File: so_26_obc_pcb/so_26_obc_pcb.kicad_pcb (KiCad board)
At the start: 4 copper layers, 90.2 x 95.9 mm, 62 parts, among them J1 Conn_02x12_Odd_Even, J2 Conn_02x06_Odd_Even, J3 Conn_01x04, J4 Conn_01x03, J5 Conn_01x03, J6 Conn_01x02, SW1 SW_Push, U1 STM32G431RBTx, U2 MPRLS0025, U3 PCT2075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

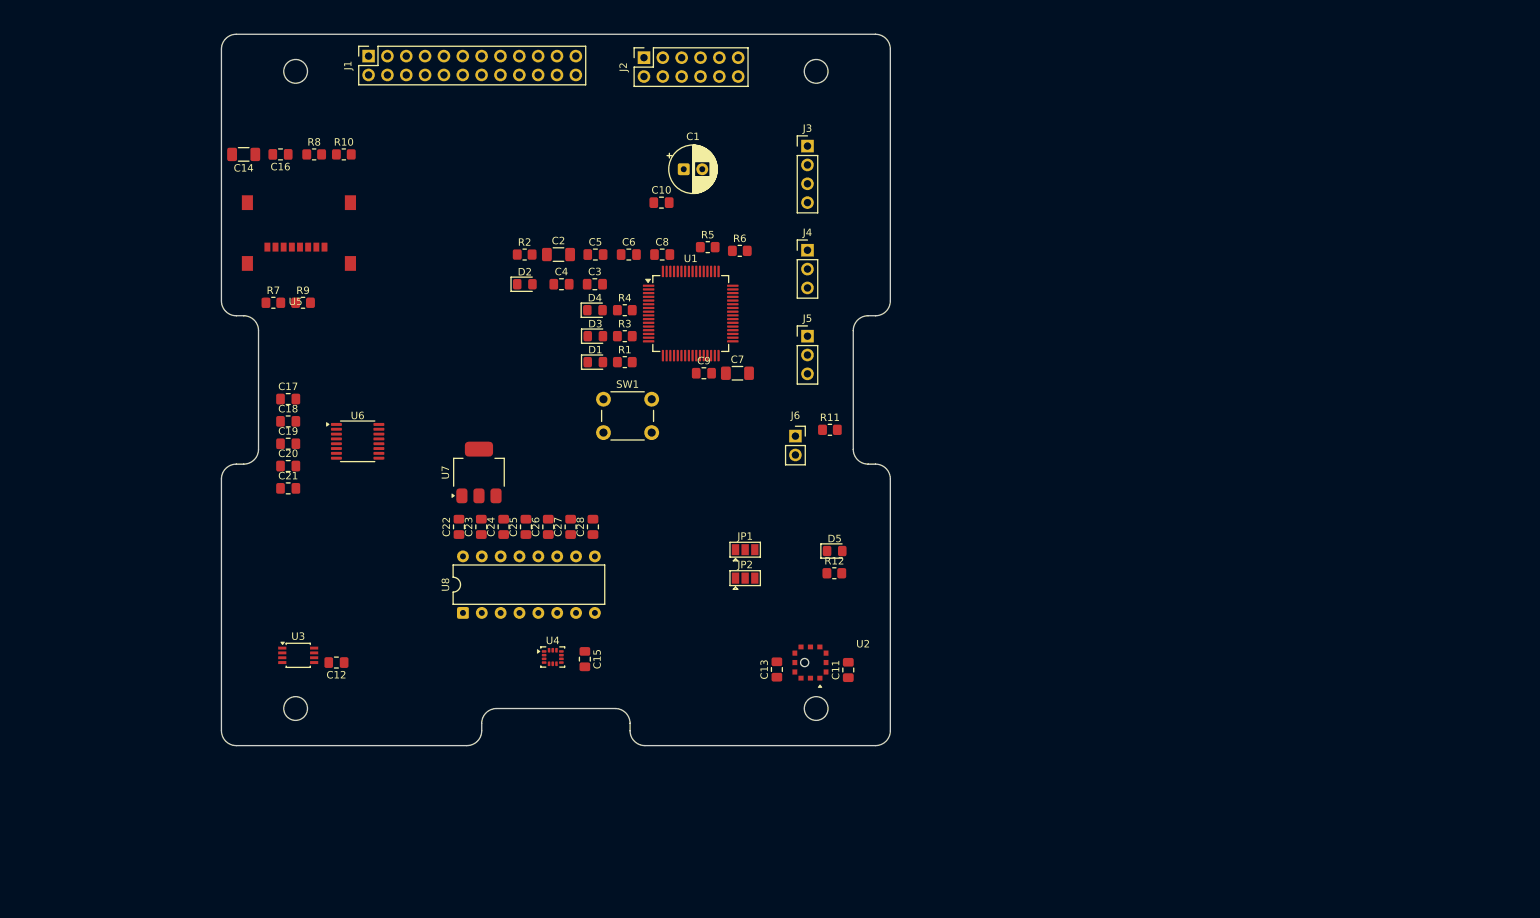
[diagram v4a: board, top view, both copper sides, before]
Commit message: changed back to old rs232 tranceiver
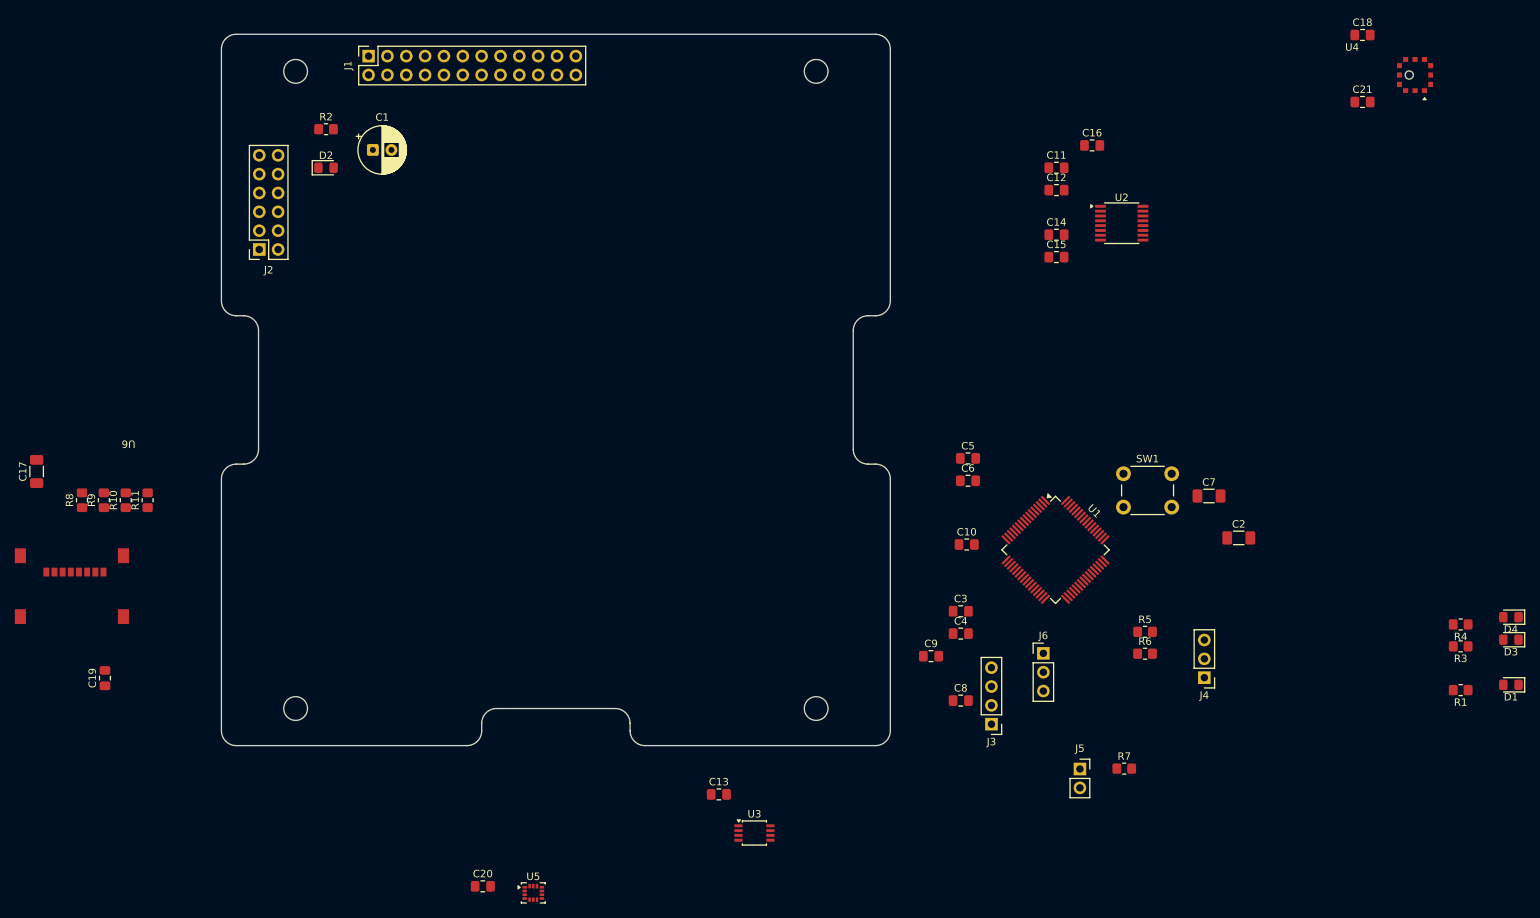
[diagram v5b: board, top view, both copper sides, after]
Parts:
- removed C22: 100n, Capacitor_SMD:C_0805_2012Metric_Pad1.18x1.45mm_HandSolder
- removed C23, C24, C25, C26: 1u, Capacitor_SMD:C_0805_2012Metric_Pad1.18x1.45mm_HandSolder
- removed C27, C28: 10u, Capacitor_SMD:C_0805_2012Metric_Pad1.18x1.45mm_HandSolder
- removed D5: LED_PWR, LED_SMD:LED_0805_2012Metric_Pad1.15x1.40mm_HandSolder
- removed JP1, JP2: SolderJumper_3_Open, Jumper:SolderJumper-3_P1.3mm_Open_Pad1.0x1.5mm
- removed R12: 10k, Resistor_SMD:R_0805_2012Metric_Pad1.20x1.40mm_HandSolder
- removed U7: AMS1117-5.0, Package_TO_SOT_SMD:SOT-223-3_TabPin2
- removed U8: MAX232, Package_DIP:DIP-16_W7.62mm
- C13: value 1n -> 100n
- C14: value 10u -> 100n; footprint Capacitor_SMD:C_1206_3216Metric_Pad1.33x1.80mm_HandSolder -> Capacitor_SMD:C_0805_2012Metric_Pad1.18x1.45mm_HandSolder
- C17: value 100n -> 10u; footprint Capacitor_SMD:C_0805_2012Metric_Pad1.18x1.45mm_HandSolder -> Capacitor_SMD:C_1206_3216Metric_Pad1.33x1.80mm_HandSolder
- C21: value 100n -> 1n
- J5: value Conn_01x03 -> Conn_01x02; footprint Connector_PinHeader_2.54mm:PinHeader_1x03_P2.54mm_Vertical -> Connector_PinSocket_2.54mm:PinSocket_1x02_P2.54mm_Vertical
- J6: value Conn_01x02 -> Conn_01x03; footprint Connector_PinSocket_2.54mm:PinSocket_1x02_P2.54mm_Vertical -> Connector_PinHeader_2.54mm:PinHeader_1x03_P2.54mm_Vertical
- U2: value MPRLS0025 -> TPT3232A-TS3R; footprint so_26_obc_footprint_library:MPRLS0025PA00002A -> Package_SO:TSSOP-16_4.4x5mm_P0.65mm
- U4: value LSM6DS3 -> MPRLS0025; footprint Package_LGA:LGA-14_3x2.5mm_P0.5mm_LayoutBorder3x4y -> so_26_obc_footprint_library:MPRLS0025PA00002A
- U5: value MEM2067-02-180-00-A -> LSM6DS3; footprint so_26_obc_footprint_library:MEM2067-02-180-00-A -> Package_LGA:LGA-14_3x2.5mm_P0.5mm_LayoutBorder3x4y
- U6: value TPT3232A-TS3R -> MEM2067-02-180-00-A; footprint Package_SO:TSSOP-16_4.4x5mm_P0.65mm -> so_26_obc_footprint_library:MEM2067-02-180-00-A
- moved C18 153.9 mm to (209.8, 45.4)
- moved C21 153.9 mm to (209.8, 54.4)
- moved U4 135.2 mm to (208.4, 47.6)
- moved D1 130.9 mm to (229.8, 133.0), turned to 180 degrees
- moved R7 130.8 mm to (177.7, 144.3)
- moved D4 130.2 mm to (229.8, 123.9), turned to 180 degrees
- moved D3 130.0 mm to (229.8, 126.9), turned to 180 degrees
- moved R1 121.0 mm to (223.0, 133.7), turned to 180 degrees
- moved R4 120.4 mm to (223.0, 124.9), turned to 180 degrees
- moved R3 120.2 mm to (223.0, 127.8), turned to 180 degrees
- moved C12 116.1 mm to (168.6, 66.3), turned to 0 degrees
- moved C14 110.1 mm to (168.6, 72.3), turned to 0 degrees
- moved C16 109.4 mm to (173.4, 60.3), turned to 0 degrees
- moved C2 99.3 mm to (193.1, 113.2)
- moved R11 92.5 mm to (46.0, 108.1), turned to 90 degrees
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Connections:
- C12 pad 1: +3V3 -> Net-(U2-C1-)
- C12 pad 2: GND -> Net-(U2-C1+)
- C13 pad 1: Net-(U2-VO+) -> +3V3
- C13 pad 2: Net-(U2-VO-) -> GND
- C14 pad 1: +3V3 -> Net-(U2-C2-)
- C14 pad 2: GND -> Net-(U2-C2+)
- C15 pad 1: +3V3 -> Net-(U2-V-)
- C16 pad 1: +3V3 -> GND
- C16 pad 2: GND -> Net-(U2-V+)
- C18 pad 1: Net-(U6-V+) -> +3V3
- C19 pad 1: Net-(U6-C1-) -> +3V3
- C19 pad 2: Net-(U6-C1+) -> GND
- C20 pad 1: Net-(U6-C2-) -> +3V3
- C20 pad 2: Net-(U6-C2+) -> GND
- C21 pad 1: Net-(U6-V-) -> Net-(U4-VO+)
- C21 pad 2: GND -> Net-(U4-VO-)
- J5 pad 1: +3V3 -> /LOW_POWER_MODE
- J5 pad 2: /BOOT0 -> GND
- J6 pad 1: /LOW_POWER_MODE -> +3V3
- J6 pad 2: GND -> /BOOT0
- R10 pad 1: Net-(U5-DAT1) -> /SD_SCK
- R11 pad 1: /LOW_POWER_MODE -> Net-(U6-DAT1)
- R7 pad 1: /SD_MISO -> /LOW_POWER_MODE
- R8 pad 1: /SD_MOSI -> /SD_MISO
- R9 pad 1: /SD_SCK -> /SD_MOSI
- U2 pad 1: unconnected-(U2-SS-Pad1) -> Net-(U2-C1+)
- U2 pad 11: unconnected-(U2-NC-Pad11) -> /RADIO_UART_TX
- U2 pad 12: +3V3 -> /RADIO_UART_RX
- U2 pad 2: /I2C_SDA -> Net-(U2-V+)
- U2 pad 3: /BOOT0 -> Net-(U2-C1-)
- U2 pad 4: Net-(U2-VO+) -> Net-(U2-C2+)
- U2 pad 5: unconnected-(U2-NC-Pad5) -> Net-(U2-C2-)
- U2 pad 6: Net-(U2-VO-) -> Net-(U2-V-)
- U2 pad 8: unconnected-(U2-EOC-Pad8) -> +3V3
- U4 pad 1: GND -> unconnected-(U4-SS-Pad1)
- U4 pad 10: unconnected-(U4-NC-Pad10) -> GND
- U4 pad 2: GND -> /I2C_SDA
- U4 pad 3: GND -> /BOOT0
- U4 pad 4: unconnected-(U4-INT1-Pad4) -> Net-(U4-VO+)
- U4 pad 5: +3V3 -> unconnected-(U4-NC-Pad5)
- U4 pad 6: GND -> Net-(U4-VO-)
- U4 pad 7: GND -> unconnected-(U4-MISO-Pad7)
- U4 pad 8: +3V3 -> unconnected-(U4-EOC-Pad8)
- U5 pad 1: Net-(U5-DAT1) -> GND
- U5 pad 2: /SD_CS -> GND
- U5 pad 3: /SD_MOSI -> GND
- U5 pad 4: +3V3 -> unconnected-(U5-INT1-Pad4)
- U5 pad 5: /SD_SCK -> +3V3
- U5 pad 7: /SD_MISO -> GND
- U5 pad 8: Net-(U5-DAT1) -> +3V3
- U6 pad 1: Net-(U6-C1+) -> Net-(U6-DAT1)
- U6 pad 2: Net-(U6-V+) -> /SD_CS
- U6 pad 3: Net-(U6-C1-) -> /SD_MOSI
- U6 pad 4: Net-(U6-C2+) -> +3V3
- U6 pad 5: Net-(U6-C2-) -> /SD_SCK
- U6 pad 6: Net-(U6-V-) -> GND
- U6 pad 7: unconnected-(U6-TOUT2-Pad7) -> /SD_MISO
- U6 pad 8: unconnected-(U6-RIN2-Pad8) -> Net-(U6-DAT1)

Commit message: Schematic: Added connector symbols for code debugging
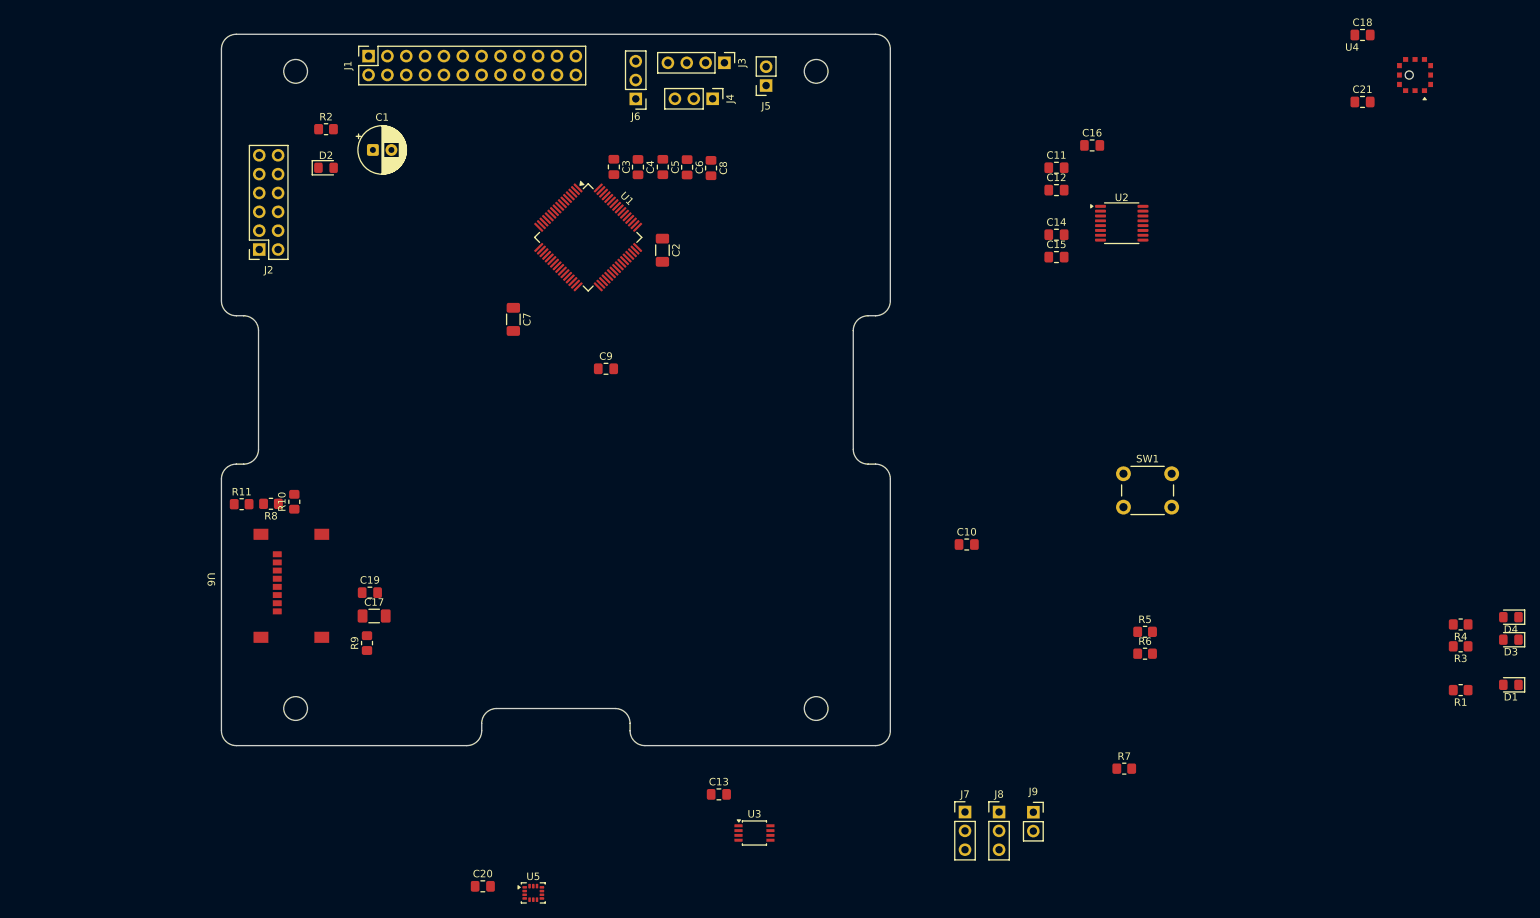
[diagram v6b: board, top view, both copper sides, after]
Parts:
- added J7: Conn_01x03, Connector_PinHeader_2.54mm:PinHeader_1x03_P2.54mm_Vertical, F.Cu at (156.2, 150.1)
- added J8: Conn_01x03, Connector_PinHeader_2.54mm:PinHeader_1x03_P2.54mm_Vertical, F.Cu at (160.8, 150.1)
- added J9: Conn_01x02, Connector_PinSocket_2.54mm:PinSocket_1x02_P2.54mm_Vertical, F.Cu at (165.4, 150.2)
- moved J4 102.4 mm to (122.2, 54.0), turned to -90 degrees
- moved J5 101.4 mm to (129.4, 52.2), turned to 180 degrees
- moved C7 96.8 mm to (95.3, 83.7), turned to -90 degrees
- moved J3 96.2 mm to (123.8, 49.1), turned to -90 degrees
- moved J6 92.8 mm to (111.8, 54.0), turned to 180 degrees
- moved C2 86.8 mm to (115.5, 74.4), turned to -90 degrees
- moved C8 79.3 mm to (122.0, 63.3), turned to -90 degrees
- moved C4 76.5 mm to (112.2, 63.2), turned to -90 degrees
- moved C3 76.0 mm to (108.9, 63.2), turned to -90 degrees
- moved U1 75.8 mm to (105.4, 72.7)
- moved C9 58.5 mm to (107.8, 90.4)
- moved C5 56.9 mm to (115.5, 63.2), turned to -90 degrees
- moved C6 56.7 mm to (118.8, 63.2), turned to -90 degrees
- moved C17 49.5 mm to (76.6, 123.7), turned to 0 degrees
- moved R9 40.4 mm to (75.6, 127.4)
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
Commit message: PCB: Placed components, did some routing
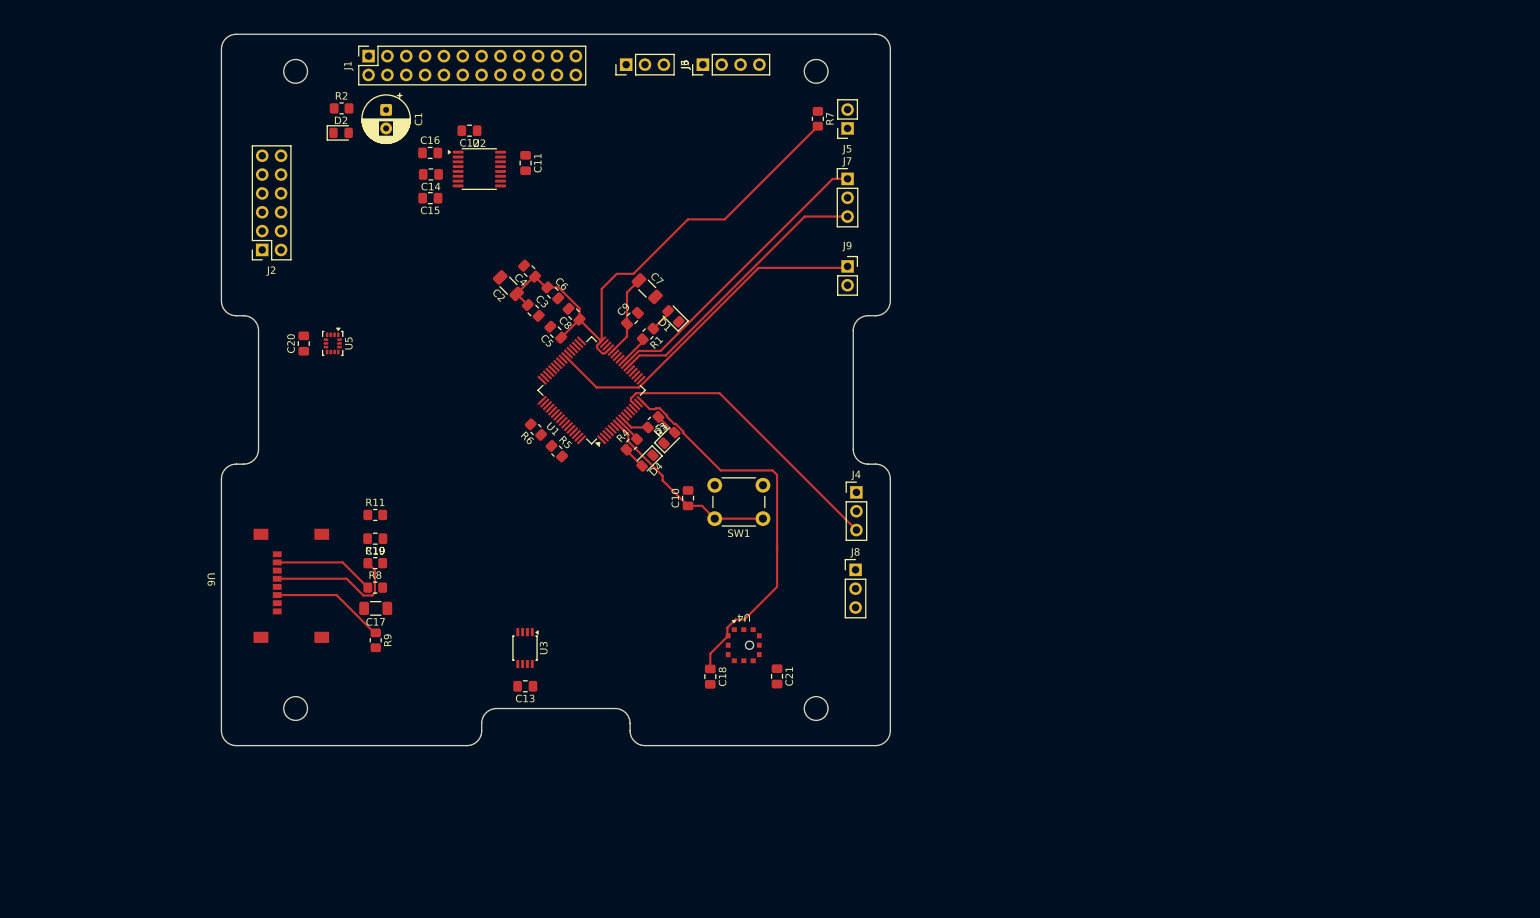
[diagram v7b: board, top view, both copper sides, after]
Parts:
- moved D1 123.3 mm to (116.9, 83.3), turned to 135 degrees
- moved C18 123.3 mm to (121.9, 131.9), turned to -90 degrees
- moved R1 119.6 mm to (113.5, 85.7), turned to -135 degrees
- moved D4 118.3 mm to (113.4, 102.8), turned to -135 degrees
- moved D3 116.7 mm to (116.4, 99.7), turned to 45 degrees
- moved R4 114.3 mm to (111.3, 100.6), turned to 45 degrees
- moved R3 113.0 mm to (114.2, 97.6), turned to -135 degrees
- moved U4 111.1 mm to (134.9, 130.9), turned to 180 degrees
- moved C21 110.6 mm to (130.9, 131.9), turned to -90 degrees
- moved R7 96.8 mm to (136.4, 56.7), turned to -90 degrees
- moved C16 89.2 mm to (84.1, 61.3)
- moved R6 87.5 mm to (98.4, 98.6), turned to 135 degrees
- moved U2 86.9 mm to (90.8, 63.5)
- moved J7 86.8 mm to (140.4, 64.8)
- moved C15 84.8 mm to (84.2, 67.4), turned to 180 degrees
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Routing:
- net +3V3: track 0.00 -> 125.2 mm
- net /PWM_HEATER: track 0.00 -> 46.5 mm
- net /RADIO_UART_RX: track 0.00 -> 40.3 mm
- net /DEBUG_UART_TX: track 0.00 -> 39.6 mm
- net /RADIO_UART_TX: track 0.00 -> 38.0 mm
- net /NRST: track 0.00 -> 26.5 mm
- net /SD_SCK: track 0.00 -> 18.6 mm
- net /SD_MOSI: track 0.00 -> 15.4 mm
- net /SD_MISO: track 0.00 -> 13.6 mm
- net Net-(U1-VREF+): track 0.00 -> 11.1 mm
- net /LED_BLUE: track 0.00 -> 4.18 mm
- net /LED_YELLOW: track 0.00 -> 3.89 mm
- net /LED_GREEN: track 0.00 -> 3.34 mm
- net Net-(D1-A): track 0.00 -> 3.22 mm
- net Net-(D4-A): track 0.00 -> 3.07 mm
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
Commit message: PCB: routing v1
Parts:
- moved R3 2.20 mm to (116.1, 98.6)
- moved D3 2.20 mm to (118.3, 100.8)
- moved D4 2.20 mm to (115.4, 103.8)
- moved R4 2.20 mm to (113.2, 101.6)
- moved C20 0.89 mm to (68.0, 87.0)
- moved C11 0.40 mm to (96.6, 62.7)
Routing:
- net +3V3: track 125.2 -> 484.6 mm, vias 0 -> 5
- net /BOOT0: track 0.00 -> 217.0 mm, vias 0 -> 7
- net /I2C_SDA: track 0.00 -> 155.8 mm, vias 0 -> 5
- net GND: track 0.00 -> 127.5 mm, vias 0 -> 70
- net /LOW_POWER_MODE: track 0.00 -> 76.7 mm, vias 0 -> 2
- net /VBAT_0: track 0.00 -> 68.8 mm, vias 0 -> 2
- net /VBAT_1: track 0.00 -> 66.4 mm, vias 0 -> 2
- net /NRST: track 26.5 -> 86.7 mm, vias 0 -> 2
- net /SWDIO: track 0.00 -> 56.4 mm, vias 0 -> 2
- net /SWCLK: track 0.00 -> 54.6 mm, vias 0 -> 2
- net /PWM_HEATER: track 46.5 -> 99.8 mm, vias 0 -> 2
- net /SD_MOSI: track 15.4 -> 66.6 mm, vias 0 -> 2
- net /SD_MISO: track 13.6 -> 62.8 mm, vias 0 -> 2
- net /SD_CS: track 0.00 -> 49.1 mm, vias 0 -> 2
- net /SD_SCK: track 18.6 -> 67.0 mm, vias 0 -> 2
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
